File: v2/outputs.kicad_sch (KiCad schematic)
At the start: 16 parts

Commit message: update hierarchy
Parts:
- added A1: Pololu_Breakout_A4988, Module:Pololu_Breakout-16_15.2x20.3mm, symbol Driver_Motor:Pololu_Breakout_A4988
- added C22: 100uF, Capacitor_THT:CP_Radial_D5.0mm_P2.50mm, symbol Device:C_Polarized_Small
- added JP1: Jumper_3_Open, Connector_PinHeader_2.54mm:PinHeader_1x03_P2.54mm_Vertical, symbol Jumper:Jumper_3_Open
- gave numbers to parts that had none: 16
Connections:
- net +12V: now also JP1.3 (B)
- net +5V: now also A1.2 (VDD), JP1.1 (A)
- net GND: now also A1.1 (GND), A1.7 (GND), C22.2
- new net: A1.8 (VMOT), C22.1, JP1.2 (C)
- new net: A1.13 (~{RESET}), A1.14 (~{SLEEP})
- new net DIR-ATTINY-A6: A1.16 (DIR)
- new net STEP-ATTINY-A5: A1.15 (STEP)
- new net SUB-A+: A1.4 (1A)
- new net SUB-A-: A1.3 (1B)
- new net SUB-B +: A1.5 (2A)
- new net SUB-B-: A1.6 (2B)
- no-connect marks 0 -> 4
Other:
- note added: "Subthrottle Driver"
- moved on the sheet: Q4

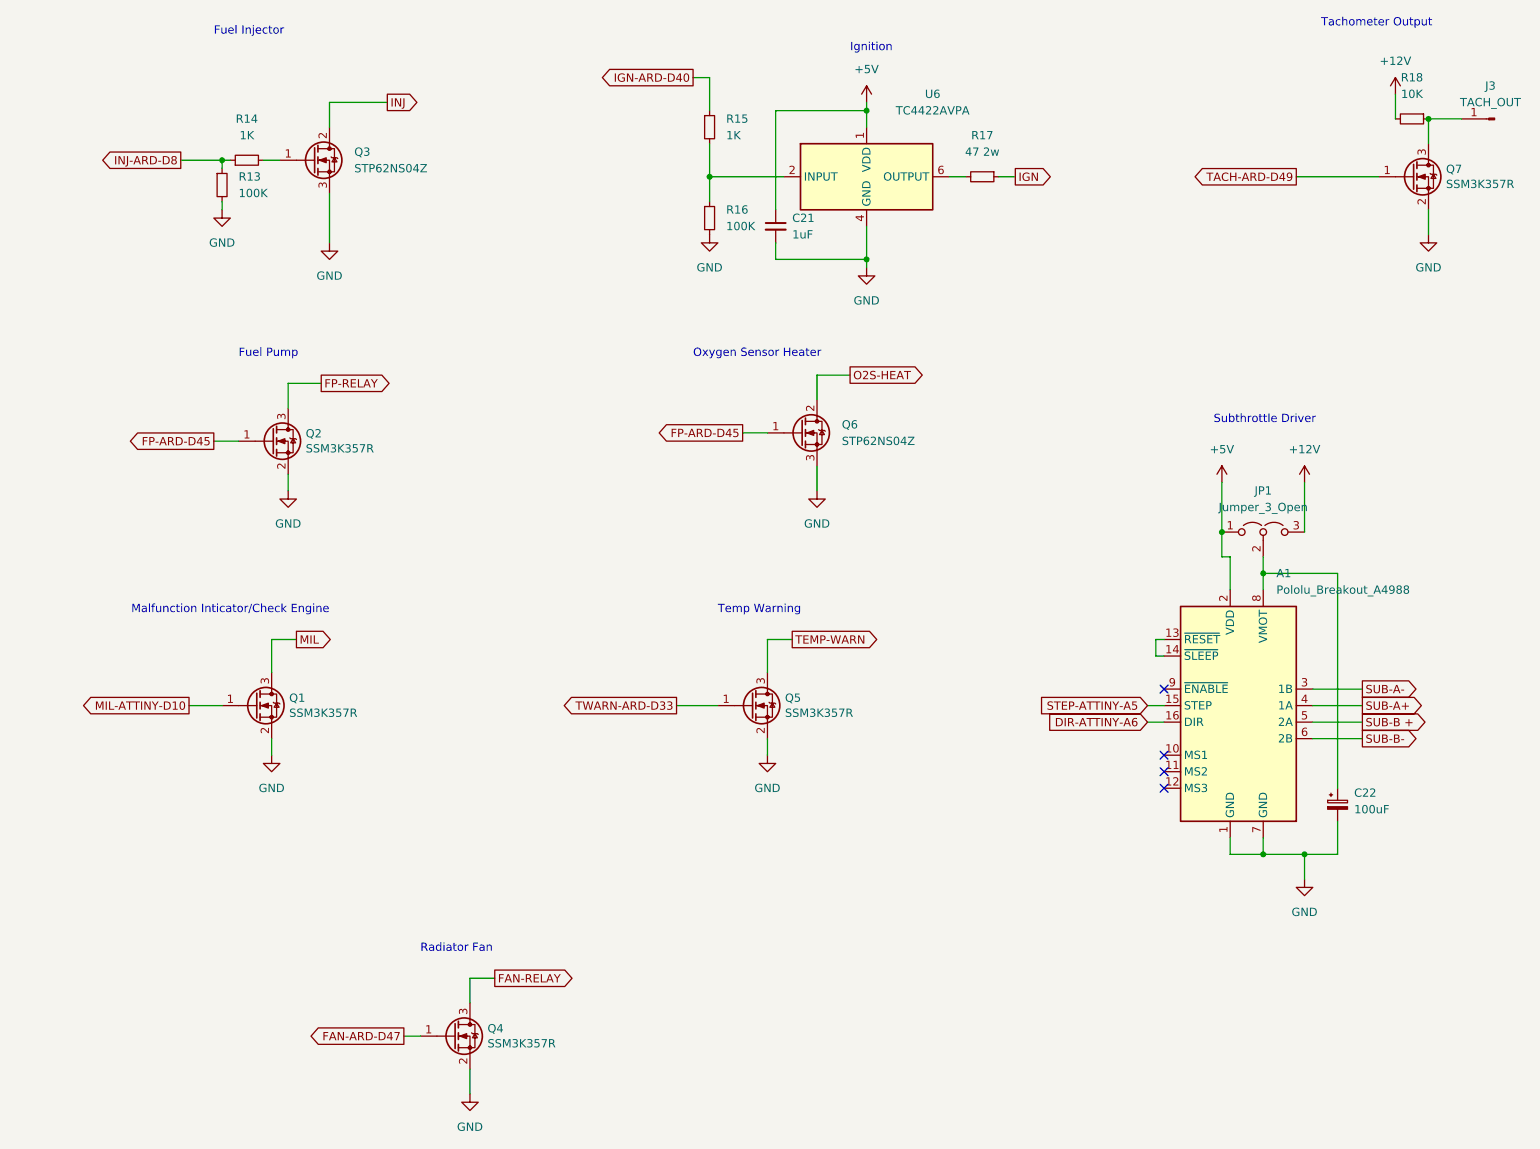
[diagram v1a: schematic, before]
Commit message: Delete ATTiny and associated circuitry
Control the secondary throttle w/ open loop stepper idle control in the speeduino firmware
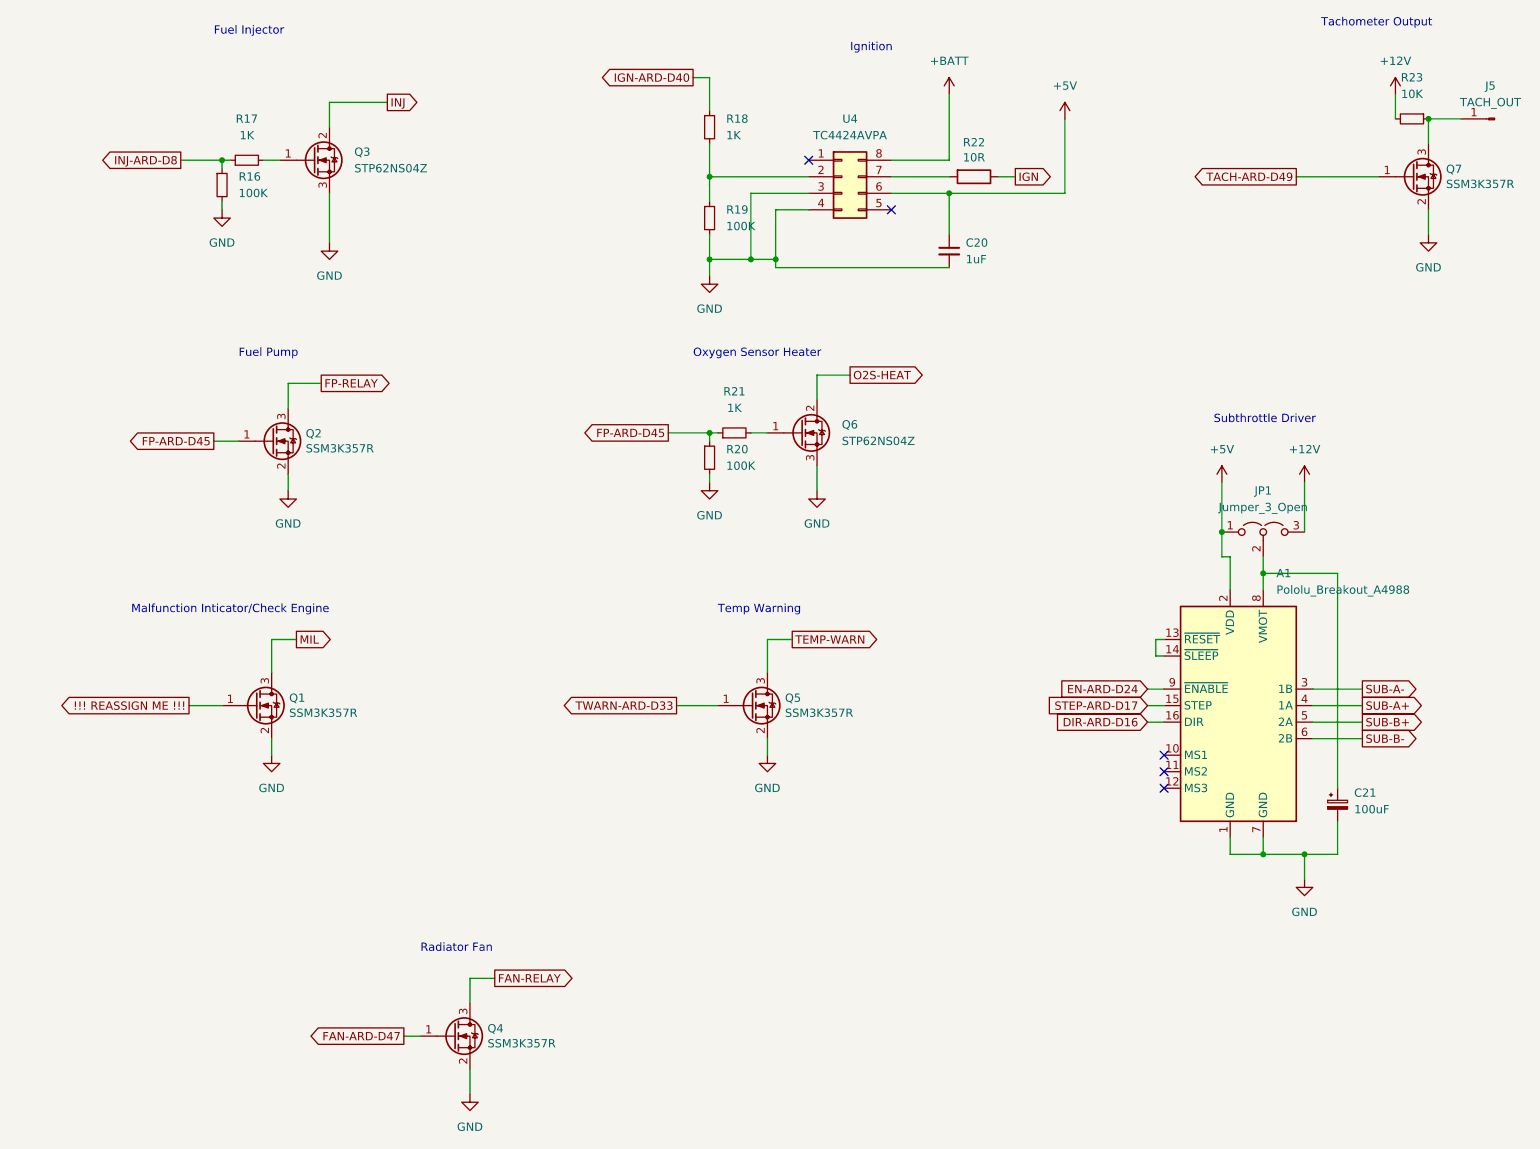
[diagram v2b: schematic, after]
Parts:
- removed R17: 47 2w, Resistor_THT:R_Axial_DIN0207_L6.3mm_D2.5mm_P5.08mm_Vertical, symbol Device:R_Small
- removed U6: TC4422AVPA, Package_DIP:DIP-8_W7.62mm, symbol Driver_FET:TC4422
- added R20: 100K, Resistor_SMD:R_0805_2012Metric, symbol Device:R_Small
- added R21: 1K, Resistor_SMD:R_0805_2012Metric, symbol Device:R_Small
- added R22: 10R, Resistor_SMD:R_0805_2012Metric, symbol Device:R
- added U4: TC4424AVPA, Package_DIP:DIP-8_W7.62mm_Socket, symbol Connector_Generic:Conn_02x04_Counter_Clockwise
- renumbered C21 to C20, C22 to C21, J3 to J5, R13 to R16, R14 to R17, R15 to R18, R16 to R19, R18 to R23
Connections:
- net +5V: now also U4.6 (Pin_6)
- net FP-ARD-D45: now also R20.1, R21.1; no longer Q6.1 (G)
- net GND: now also R20.2, U4.3 (Pin_3), U4.4 (Pin_4)
- net IGN: now also R22.1
- net at R18.2, R19.1: now also U4.2 (Pin_2)
- net EN-ARD-D24: now reaches A1.9 (~{ENABLE})
- net DIR-ATTINY-A6 renamed DIR-ARD-D16
- net MIL-ATTINY-D10 renamed !!! REASSIGN ME !!!
- net STEP-ATTINY-A5 renamed STEP-ARD-D17
- net SUB-B + renamed SUB-B+
- new net: R22.2, U4.7 (Pin_7)
- new net: Q6.1 (G), R21.2
- new net +BATT: U4.8 (Pin_8)
- no-connect marks 4 -> 5
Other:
- moved on the sheet: C20

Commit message: Reassign check engine light net
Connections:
- net !!! REASSIGN ME !!! renamed MIL-ARD-D32
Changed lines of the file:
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@@
     )
   )
-  (global_label "!!! REASSIGN ME !!!" (shape output) (at 53.34 120.65 180) (fields_autoplaced)
+  (global_label "MIL-ARD-D32" (shape output) (at 53.34 120.65 180) (fields_autoplaced)
     (effects (font (size 1.27 1.27)) (justify right))
-    (property "Intersheet References" "${INTERSHEET_REFS}" (id 0) (at 32.6631 120.5706 0)
+    (property "Intersheet References" "${INTERSHEET_REFS}" (id 0) (at 37.3802 120.5706 0)
       (effects (font (size 1.27 1.27)) (justify right) hide)
     )

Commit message: V2.1 is done?
Uses the JST WPZ connector footprint instead of standard
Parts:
- removed Q6: STP62NS04Z, Package_TO_SOT_THT:TO-220-3_Vertical, symbol Transistor_FET:BUZ11
- removed R20: 100K, Resistor_SMD:R_0805_2012Metric, symbol Device:R_Small
- removed R21: 1K, Resistor_SMD:R_0805_2012Metric, symbol Device:R_Small
- renumbered Q7 to Q6, R22 to R20, R23 to R21
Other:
- note removed: "Oxygen Sensor Heater"

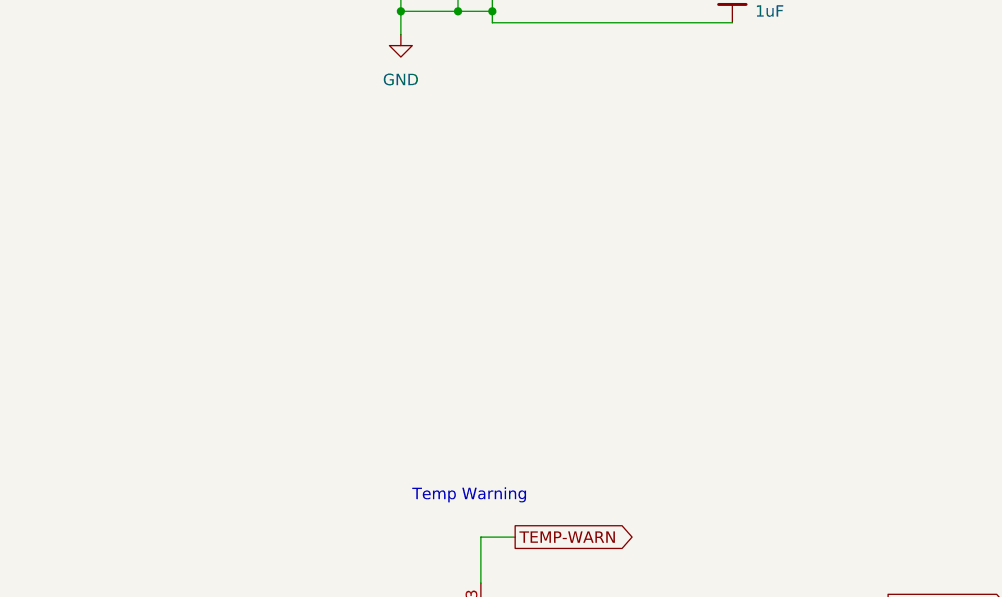
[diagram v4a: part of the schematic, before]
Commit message: Add control of air switching valve
Plus a jumper to lock the valve closed
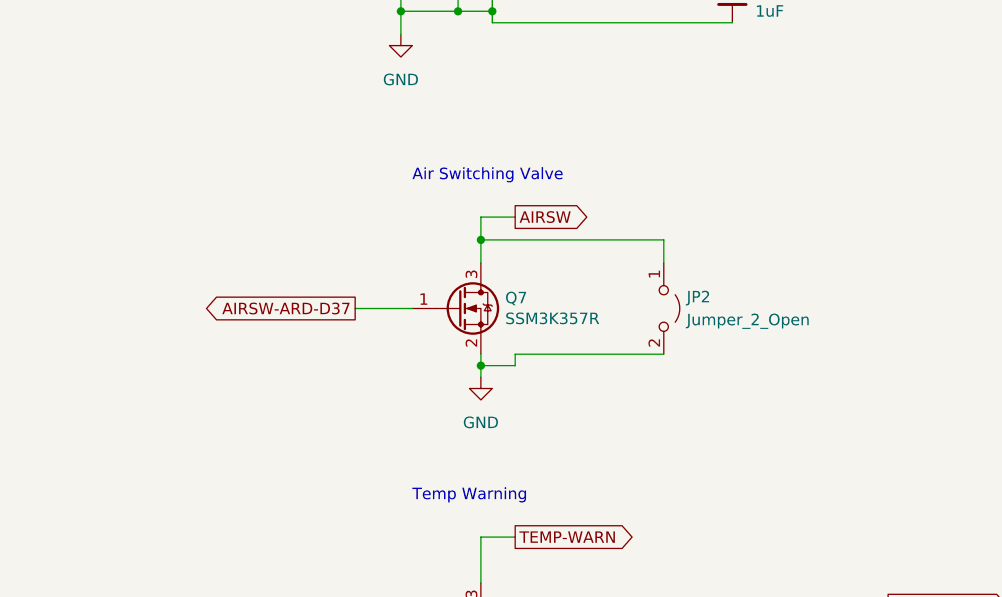
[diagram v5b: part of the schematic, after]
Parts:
- added JP2: Jumper_2_Open, Connector_PinHeader_2.54mm:PinHeader_1x02_P2.54mm_Vertical, symbol Jumper:Jumper_2_Open
- added Q7: SSM3K357R, Package_TO_SOT_SMD:SOT-23, symbol Transistor_FET:2N7002
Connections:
- net GND: now also JP2.2 (B), Q7.2 (S)
- new net AIRSW: JP2.1 (A), Q7.3 (D)
- new net AIRSW-ARD-D37: Q7.1 (G)
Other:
- note added: "Air Switching Valve"
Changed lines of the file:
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@@
   (junction (at 58.42 36.83) (diameter 0) (color 0 0 0 0)
   )
+  (junction (at 142.24 77.47) (diameter 0) (color 0 0 0 0)
+  )
   (junction (at 218.44 143.51) (diameter 0) (color 0 0 0 0)
   )
@@
   )
   (junction (at 133.35 39.37) (diameter 0) (color 0 0 0 0)
+  )
+  (junction (at 142.24 91.44) (diameter 0) (color 0 0 0 0)
   )
   (junction (at 133.35 52.07) (diameter 0) (color 0 0 0 0)
@@
     (stroke (width 0) (type default) (color 0 0 0 0))
   )
+  (wire (pts (xy 142.24 77.47) (xy 142.24 80.01))
+    (stroke (width 0) (type default) (color 0 0 0 0))
+  )
   (wire (pts (xy 68.58 71.12) (xy 73.66 71.12))
     (stroke (width 0) (type default) (color 0 0 0 0))
@@
     (stroke (width 0) (type default) (color 0 0 0 0))
   )
+  (wire (pts (xy 162.56 77.47) (xy 162.56 80.01))
+    (stroke (width 0) (type default) (color 0 0 0 0))
+  )
   (wire (pts (xy 53.34 120.65) (xy 58.42 120.65))
     (stroke (width 0) (type default) (color 0 0 0 0))
@@
     (stroke (width 0) (type default) (color 0 0 0 0))
   )
+  (wire (pts (xy 142.24 74.93) (xy 142.24 77.47))
+    (stroke (width 0) (type default) (color 0 0 0 0))
+  )
   (wire (pts (xy 143.51 44.45) (xy 148.59 44.45))
     (stroke (width 0) (type default) (color 0 0 0 0))
@@
     (stroke (width 0) (type default) (color 0 0 0 0))
   )
+  (wire (pts (xy 146.05 90.17) (xy 146.05 91.44))
+    (stroke (width 0) (type default) (color 0 0 0 0))
+  )
   (wire (pts (xy 170.18 36.83) (xy 170.18 26.67))
     (stroke (width 0) (type default) (color 0 0 0 0))
   )
+  (wire (pts (xy 142.24 77.47) (xy 162.56 77.47))
+    (stroke (width 0) (type default) (color 0 0 0 0))
+  )
   (wire (pts (xy 213.36 143.51) (xy 218.44 143.51))
     (stroke (width 0) (type default) (color 0 0 0 0))
@@
     (stroke (width 0) (type default) (color 0 0 0 0))
   )
+  (wire (pts (xy 128.27 85.09) (xy 134.62 85.09))
+    (stroke (width 0) (type default) (color 0 0 0 0))
+  )
+  (wire (pts (xy 162.56 90.17) (xy 146.05 90.17))
+    (stroke (width 0) (type default) (color 0 0 0 0))
+  )
+  (wire (pts (xy 146.05 91.44) (xy 142.24 91.44))
+    (stroke (width 0) (type default) (color 0 0 0 0))
+  )
+  (wire (pts (xy 142.24 90.17) (xy 142.24 91.44))
+    (stroke (width 0) (type default) (color 0 0 0 0))
+  )
   (wire (pts (xy 213.36 97.79) (xy 212.09 97.79))
     (stroke (width 0) (type default) (color 0 0 0 0))
@@
     (stroke (width 0) (type default) (color 0 0 0 0))
   )
+  (wire (pts (xy 142.24 91.44) (xy 142.24 92.71))
+    (stroke (width 0) (type default) (color 0 0 0 0))
+  )
   (wire (pts (xy 69.85 110.49) (xy 66.04 110.49))
     (stroke (width 0) (type default) (color 0 0 0 0))
@@
     (stroke (width 0) (type default) (color 0 0 0 0))
   )
+  (wire (pts (xy 146.05 74.93) (xy 142.24 74.93))
+    (stroke (width 0) (type default) (color 0 0 0 0))
+  )
   (wire (pts (xy 66.04 110.49) (xy 66.04 115.57))
     (stroke (width 0) (type default) (color 0 0 0 0))
@@
     (effects (font (size 1.27 1.27)) (justify left bottom))
   )
+  (text "Air Switching Valve" (at 134.62 71.12 0)
+    (effects (font (size 1.27 1.27)) (justify left bottom))
+  )
   (text "Temp Warning" (at 134.62 106.68 0)
     (effects (font (size 1.27 1.27)) (justify left bottom))
@@
     )
   )
+  (global_label "AIRSW-ARD-D37" (shape output) (at 128.27 85.09 180) (fields_autoplaced)
+    (effects (font (size 1.27 1.27)) (justify right))
+    (property "Intersheet References" "${INTERSHEET_REFS}" (id 0) (at 109.7702 85.0106 0)
+      (effects (font (size 1.27 1.27)) (justify right) hide)
+    )
+  )
   (global_label "FP-ARD-D45" (shape output) (at 57.15 80.01 180) (fields_autoplaced)
     (effects (font (size 1.27 1.27)) (justify right))
@@
     (property "Intersheet References" "${INTERSHEET_REFS}" (id 0) (at 37.5012 36.7506 0)
       (effects (font (size 1.27 1.27)) (justify right) hide)
+    )
+  )
+  (global_label "AIRSW" (shape output) (at 146.05 74.93 0) (fields_autoplaced)
+    (effects (font (size 1.27 1.27)) (justify left))
+    (property "Intersheet References" "${INTERSHEET_REFS}" (id 0) (at 154.0874 74.8506 0)
+      (effects (font (size 1.27 1.27)) (justify left) hide)
     )
   )
@@
     )
     (pin "1")
+  )
+  (symbol (lib_id "Transistor_FET:2N7002") (at 139.7 85.09 0) (unit 1)
+    (in_bom yes) (on_board yes)
+    (property "Reference" "Q7" (id 0) (at 144.9324 83.9216 0)
+      (effects (font (size 1.27 1.27)) (justify left))
+    )
+    (property "Value" "SSM3K357R" (id 1) (at 144.9324 86.233 0)
+      (effects (font (size 1.27 1.27)) (justify left))
+    )
+    (property "Footprint" "Package_TO_SOT_SMD:SOT-23" (id 2) (at 144.78 86.995 0)
+      (effects (font (size 1.27 1.27) italic) (justify left) hide)
+    )
+    (property "Datasheet" "https://www.mouser.com/datasheet/2/408/SSM3K357R_datasheet_en_20180124-1316146.pdf" (id 3) (at 139.7 85.09 0)
+      (effects (font (size 1.27 1.27)) (justify left) hide)
+    )
+    (property "Digikey Part Number" "SSM3K357RLFCT-ND " (id 4) (at 1.27 179.07 0)
+      (effects (font (size 1.27 1.27)) hide)
+    )
+    (property "Manufacturer_Name" "Toshiba" (id 5) (at 1.27 179.07 0)
+      (effects (font (size 1.27 1.27)) hide)
+    )
+    (property "Manufacturer_Part_Number" "SSM3K357R" (id 6) (at 1.27 179.07 0)
+      (effects (font (size 1.27 1.27)) hide)
+    )
+    (property "URL" "https://www.digikey.com.au/product-detail/en/toshiba-semiconductor-and-storage/SSM3K357RLF/SSM3K357RLFCT-ND/8611183" (id 7) (at 1.27 179.07 0)
+      (effects (font (size 1.27 1.27)) hide)
+    )
+    (pin "1")
+    (pin "2")
+    (pin "3")
   )
   (symbol (lib_id "power:+12V") (at 224.79 86.36 0) (unit 1)
@@
     (pin "9")
   )
+  (symbol (lib_id "Jumper:Jumper_2_Open") (at 162.56 85.09 270) (unit 1)
+    (in_bom yes) (on_board yes) (fields_autoplaced)
+    (property "Reference" "JP2" (id 0) (at 165.1 83.8199 90)
+      (effects (font (size 1.27 1.27)) (justify left))
+    )
+    (property "Value" "Jumper_2_Open" (id 1) (at 165.1 86.3599 90)
+      (effects (font (size 1.27 1.27)) (justify left))
+    )
+    (property "Footprint" "Connector_PinHeader_2.54mm:PinHeader_1x02_P2.54mm_Vertical" (id 2) (at 162.56 85.09 0)
+      (effects (font (size 1.27 1.27)) hide)
+    )
+    (property "Datasheet" "~" (id 3) (at 162.56 85.09 0)
+      (effects (font (size 1.27 1.27)) hide)
+    )
+    (pin "1")
+    (pin "2")
+  )
   (symbol (lib_id "power:GND") (at 68.58 87.63 0) (unit 1)
     (in_bom yes) (on_board yes) (fields_autoplaced)
@@
       (effects (font (size 1.27 1.27)) hide)
     )
+    (pin "1")
+  )
+  (symbol (lib_id "power:GND") (at 142.24 92.71 0) (unit 1)
+    (in_bom yes) (on_board yes) (fields_autoplaced)
+    (property "Reference" "#PWR048" (id 0) (at 142.24 99.06 0)
+      (effects (font (size 1.27 1.27)) hide)
+    )
+    (property "Value" "GND" (id 1) (at 142.24 97.79 0))
+    (property "Footprint" "" (id 2) (at 142.24 92.71 0)
+      (effects (font (size 1.27 1.27)) hide)
+    )
+    (property "Datasheet" "" (id 3) (at 142.24 92.71 0)
+      (effects (font (size 1.27 1.27)) hide)
+    )
